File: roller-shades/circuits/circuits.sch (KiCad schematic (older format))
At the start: 24 parts, among them U1 AMS1117-3.3, U3 ESP-12F

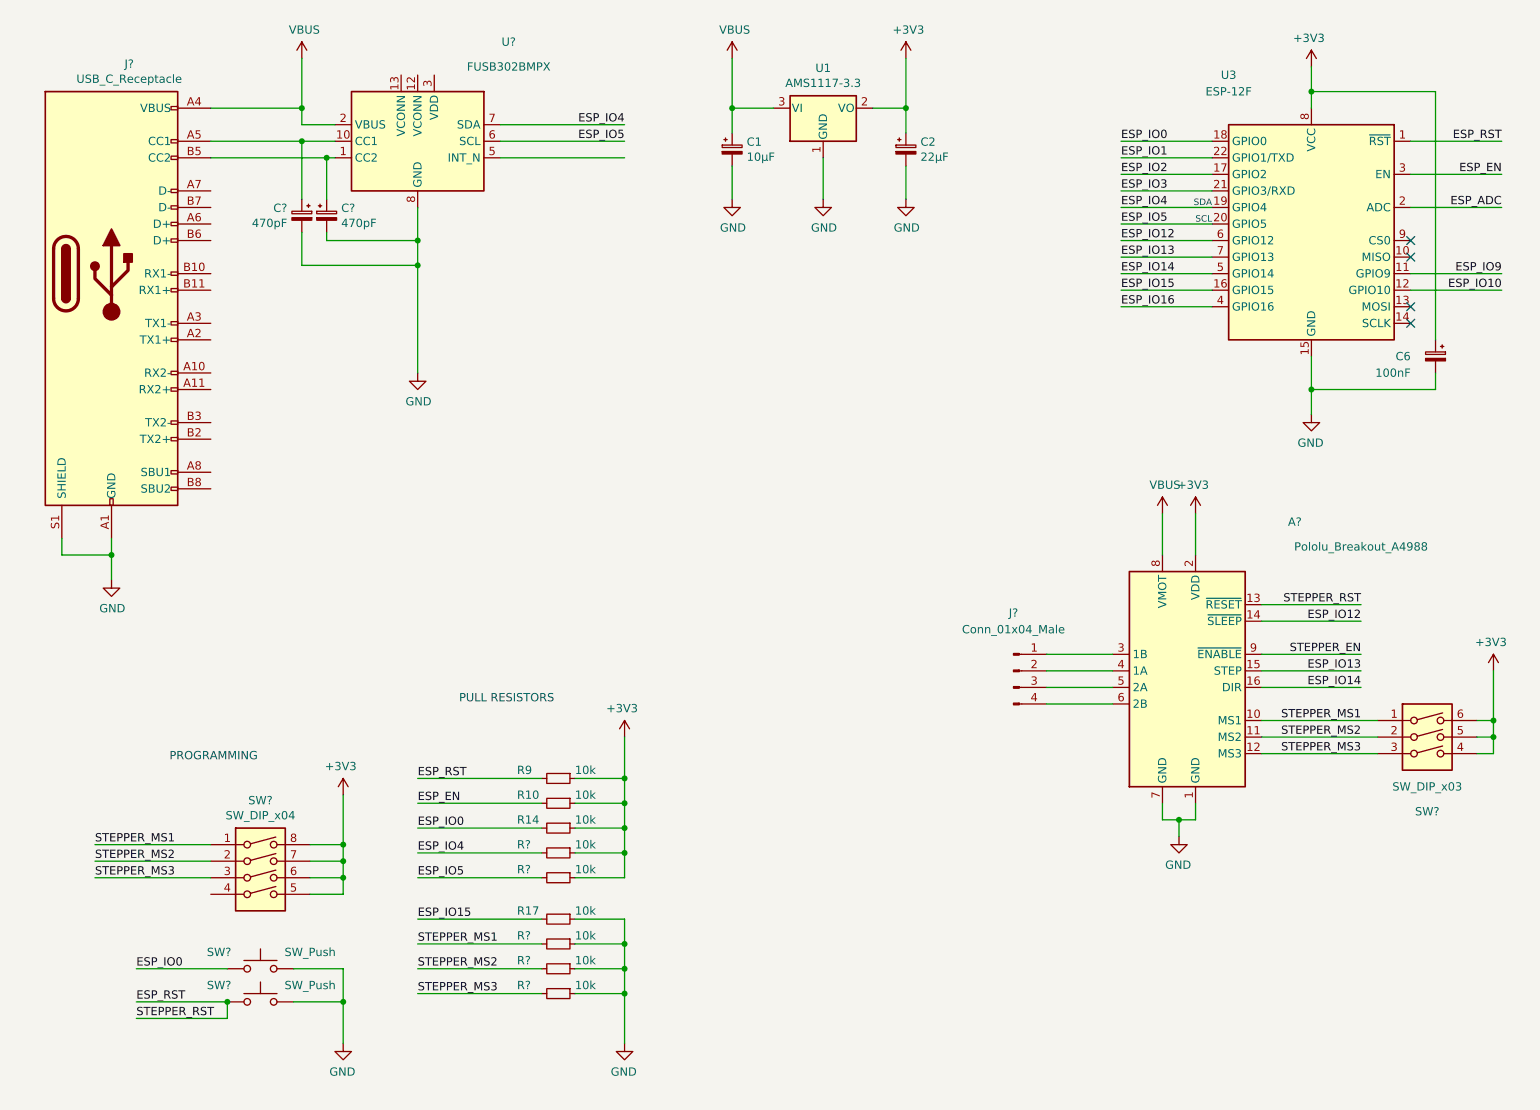
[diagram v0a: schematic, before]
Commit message: Refractored KiCAD repo libraries and added AS5601-ASOM
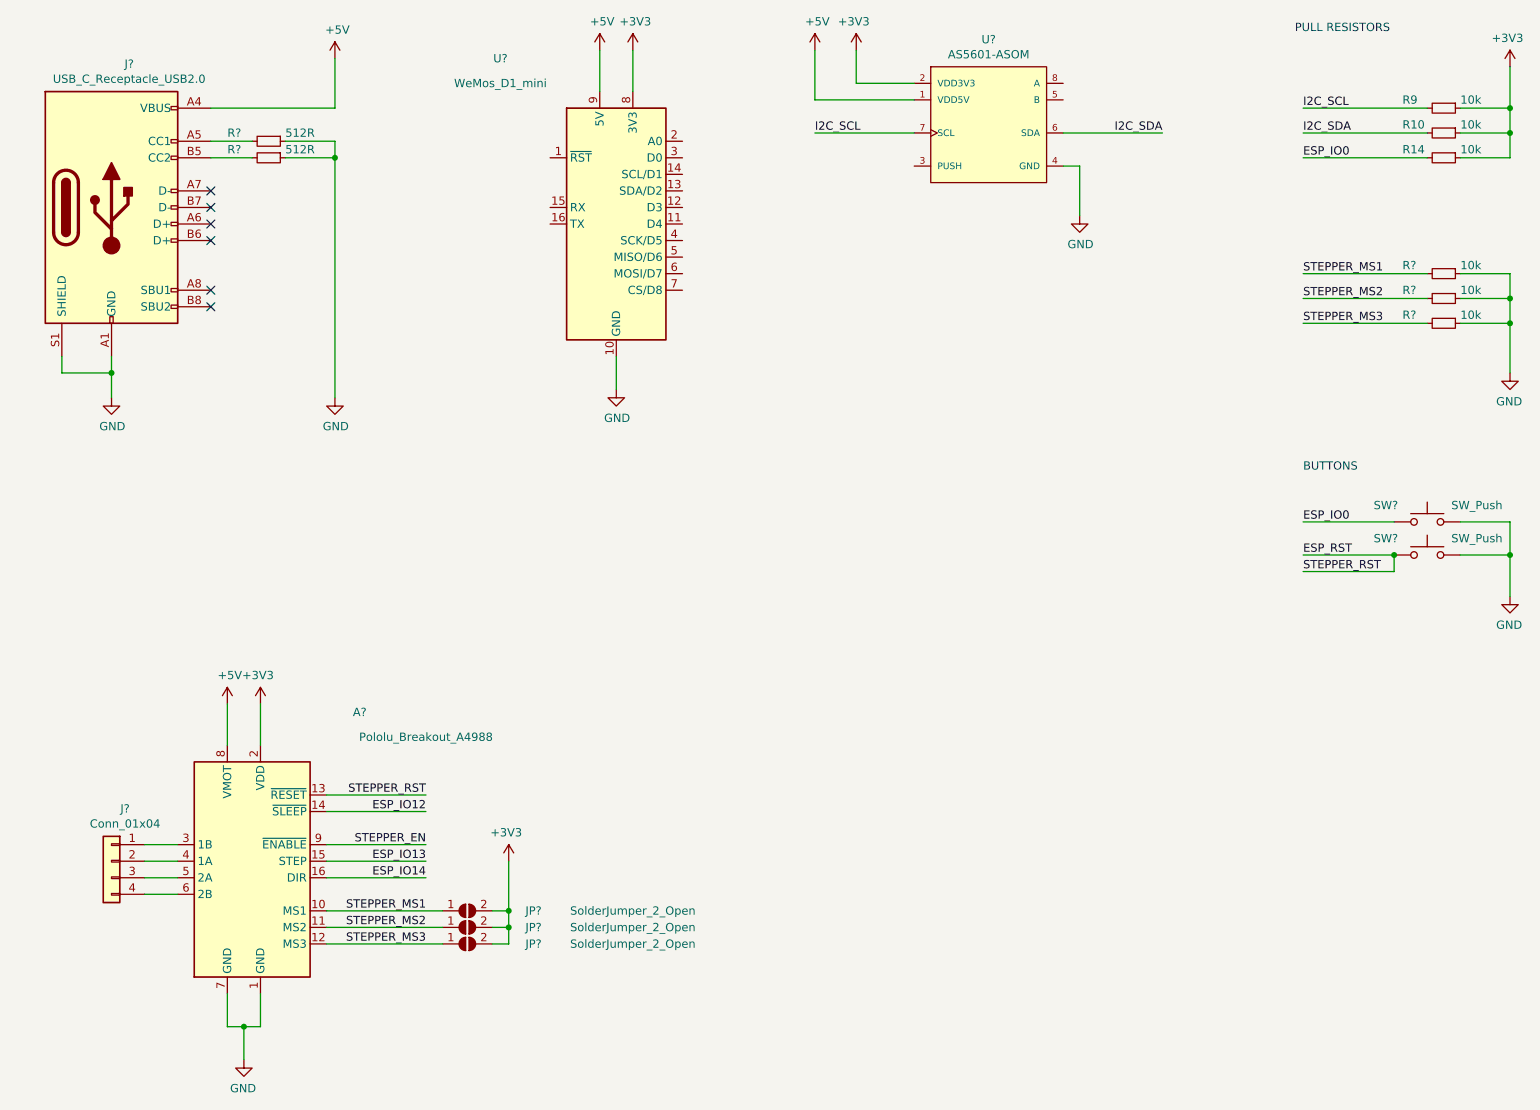
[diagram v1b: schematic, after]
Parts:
- removed C1: 10µF, Capacitor_SMD:C_1206_3216Metric, symbol Device:CP_Small
- removed C2: 22µF, Capacitor_SMD:C_1206_3216Metric, symbol Device:CP_Small
- removed C6: 100nF, Capacitor_SMD:C_1206_3216Metric, symbol Device:CP_Small
- removed C? (x2): 470pF, Capacitor_SMD:C_1206_3216Metric, symbol Device:CP_Small
- removed J?: Conn_01x04_Male, symbol Connector:Conn_01x04_Male
- removed J?: USB_C_Receptacle, symbol Connector:USB_C_Receptacle
- removed R17, R? (x2): 10k, Capacitor_SMD:C_1206_3216Metric, symbol Device:R_Small
- removed SW?: SW_DIP_x04, symbol Switch:SW_DIP_x04
- removed SW?: SW_DIP_x03, symbol Switch:SW_DIP_x03
- removed U1: AMS1117-3.3, Package_TO_SOT_SMD:SOT-223-3_TabPin2, symbol Regulator_Linear:AMS1117-3.3
- removed U3: ESP-12F, RF_Module:ESP-12E, symbol RF_Module:ESP-12F
- removed U?: FUSB302BMPX, Package_DFN_QFN:WQFN-14-1EP_2.5x2.5mm_P0.5mm_EP1.45x1.45mm, symbol Interface_USB:FUSB302BMPX
- added J?: USB_C_Receptacle_USB2.0, symbol Connector:USB_C_Receptacle_USB2.0
- added J?: Conn_01x04, symbol Connector_Generic:Conn_01x04
- added JP? (x3): SolderJumper_2_Open, symbol Jumper:SolderJumper_2_Open
- added R? (x2): 512R, Capacitor_SMD:C_1206_3216Metric, symbol Device:R_Small
- added U?: WeMos_D1_mini, Module:WEMOS_D1_mini_light, symbol MCU_Module:WeMos_D1_mini
- added U?: AS5601-ASOM, Taos-AS5601-ASOM-0-0-*, symbol AS5601:AS5601-ASOM
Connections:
- net +3V3: now also JP?.2 (B), JP?.2 (B), JP?.2 (B), U?.2 (VDD3V3), U?.8 (3V3)
- net ESP_RST: no longer R9.2
- net GND: now also J?.A1 (GND), J?.A12 (GND), J?.B1 (GND), J?.B12 (GND), J?.S1 (SHIELD), R?.1, R?.1, U?.10 (GND), U?.4 (GND)
- net STEPPER_MS1: now also JP?.1 (A)
- net STEPPER_MS2: now also JP?.1 (A)
- net STEPPER_MS3: now also JP?.1 (A)
- net at A?.3 (1B): now also J?.1 (Pin_1)
- net at A?.4 (1A): now also J?.2 (Pin_2)
- net at A?.5 (2A): now also J?.3 (Pin_3)
- net at A?.6 (2B): now also J?.4 (Pin_4)
- net ESP_EN renamed I2C_SDA
- net I2C_SDA: now also U?.6 (SDA)
- net VBUS renamed +5V
- net +5V: now also J?.A4 (VBUS), J?.A9 (VBUS), J?.B4 (VBUS), J?.B9 (VBUS), U?.1 (VDD5V), U?.9 (5V)
- new net: J?.A5 (CC1), R?.2
- new net: J?.B5 (CC2), R?.2
- new net I2C_SCL: R9.2, U?.7 (SCL)
- no-connect marks 4 -> 6
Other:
- note added: "BUTTONS"
- note removed: "PROGRAMMING"
- note removed: "SCL"
- note removed: "SDA"
- moved on the sheet: A?, R10, R14, R9, R?, SW?

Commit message: work on roller shade schmatics
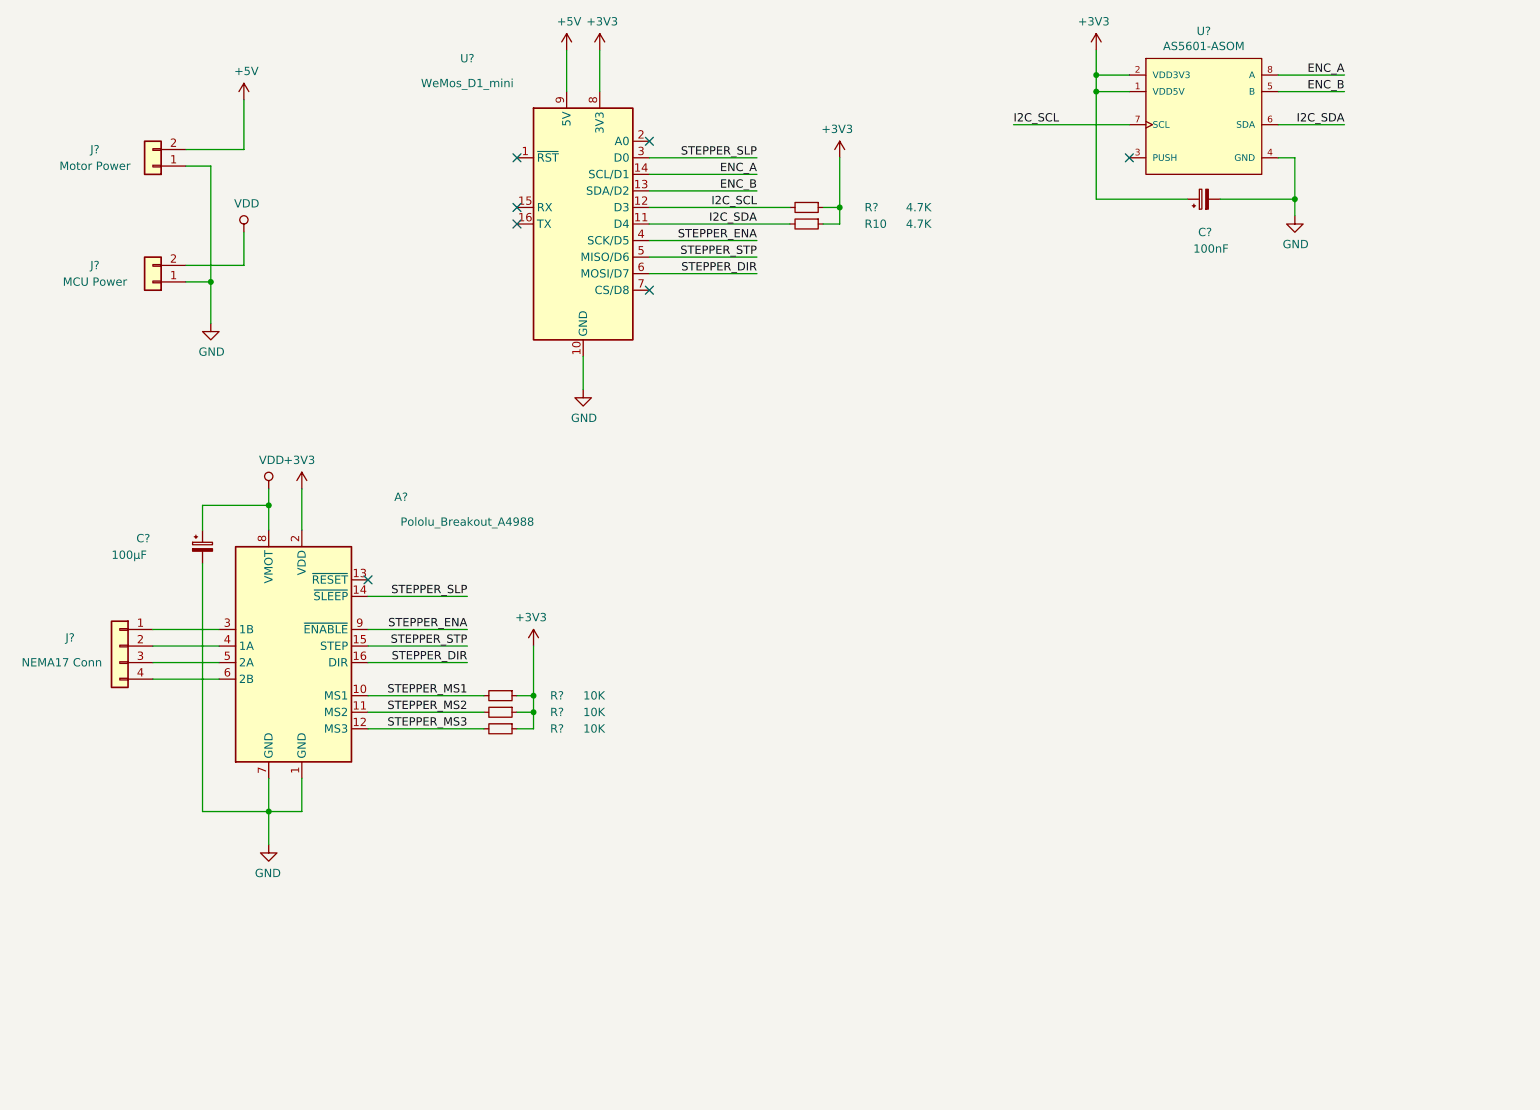
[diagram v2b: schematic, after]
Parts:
- removed J?: USB_C_Receptacle_USB2.0, symbol Connector:USB_C_Receptacle_USB2.0
- removed JP? (x3): SolderJumper_2_Open, symbol Jumper:SolderJumper_2_Open
- removed R14, R9, R? (x3): 10k, Capacitor_SMD:C_1206_3216Metric, symbol Device:R_Small
- removed R? (x2): 512R, Capacitor_SMD:C_1206_3216Metric, symbol Device:R_Small
- removed SW? (x2): SW_Push, symbol Switch:SW_Push
- added C?: 100µF, symbol Device:CP_Small
- added C?: 100nF, symbol Device:CP_Small
- added J?: Motor Power, symbol Connector_Generic:Conn_01x02
- added J?: MCU Power, symbol Connector_Generic:Conn_01x02
- added R?: 4.7K, Capacitor_SMD:C_1206_3216Metric, symbol Device:R_Small
- added R? (x3): 10K, Capacitor_SMD:C_1206_3216Metric, symbol Device:R_Small
- J?: value Conn_01x04 -> NEMA17 Conn
- R10: value 10k -> 4.7K
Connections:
- net ESP_IO12 is gone; now on net STEPPER_SLP: A?.14 (~SLEEP)
- net ESP_IO13 is gone; now on net STEPPER_STP: A?.15 (STEP)
- net ESP_IO14 is gone; now on net STEPPER_DIR: A?.16 (DIR)
- net STEPPER_EN is gone; now on net STEPPER_ENA: A?.9 (~ENABLE)
- net +3V3: now also U?.1 (VDD5V), C?.1, R?.1, R?.1, R?.1, R?.1
- net +5V: now also J?.2 (Pin_2); no longer A?.8 (VMOT), U?.1 (VDD5V)
- net GND: now also C?.2, C?.2, J?.1 (Pin_1), J?.1 (Pin_1)
- net I2C_SCL: now also U?.12 (D3), R?.2
- net I2C_SDA: now also U?.11 (D4)
- net STEPPER_MS1: now also R?.2
- net STEPPER_MS2: now also R?.2
- net STEPPER_MS3: now also R?.2
- net ENC_B: now reaches U?.13 (SDA/D2)
- net ENC_B: now also U?.5 (B)
- net ENC_A: now reaches U?.14 (SCL/D1)
- net ENC_A: now also U?.8 (A)
- net STEPPER_SLP: now reaches U?.3 (D0)
- net STEPPER_ENA: now reaches U?.4 (SCK/D5)
- net STEPPER_STP: now reaches U?.5 (MISO/D6)
- net STEPPER_DIR: now reaches U?.6 (MOSI/D7)
- net ESP_RST: no longer names the net of A?.13 (~RESET)
- new net VDD: A?.8 (VMOT), C?.1, J?.2 (Pin_2)
- no-connect marks 6 -> 7
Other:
- note removed: "BUTTONS"
- note removed: "PULL RESISTORS"
- moved on the sheet: A?, J?, R10, U?

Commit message: working on driver board using kicad stepup for freecad
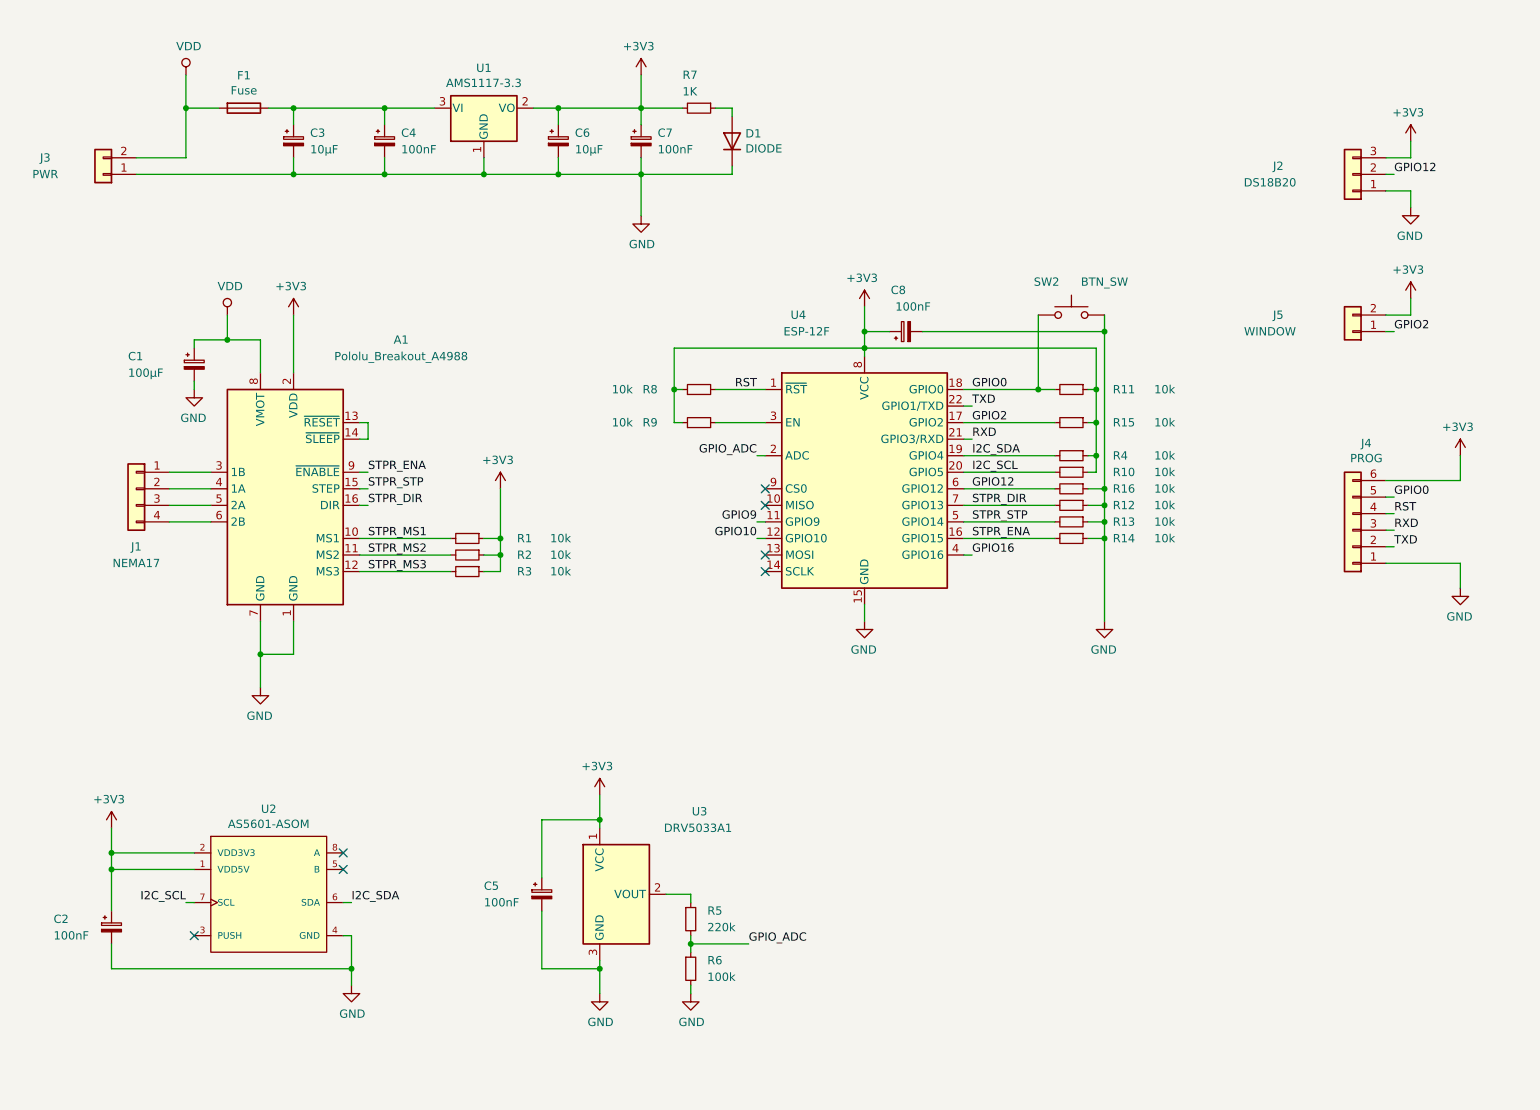
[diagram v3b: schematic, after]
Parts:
- removed J?: Motor Power, symbol Connector_Generic:Conn_01x02
- removed U?: WeMos_D1_mini, Module:WEMOS_D1_mini_light, symbol MCU_Module:WeMos_D1_mini
- added C3, C6: 10µF, Capacitor_SMD:C_0603_1608Metric, symbol Device:CP_Small
- added C4, C5, C7: 100nF, Capacitor_SMD:C_0603_1608Metric, symbol Device:CP_Small
- added C8: 100nF, Fuse:Fuse_0805_2012Metric, symbol Device:CP_Small
- added D1: DIODE, Diode_SMD:D_0805_2012Metric, symbol Simulation_SPICE:DIODE
- added F1: Fuse, Fuse:Fuse_0603_1608Metric, symbol Device:Fuse
- added J2: DS18B20, Connector_PinSocket_2.00mm:PinSocket_1x03_P2.00mm_Vertical, symbol Connector_Generic:Conn_01x03
- added J4: PROG, Connector_PinHeader_2.00mm:PinHeader_1x06_P2.00mm_Vertical, symbol Connector_Generic:Conn_01x06
- added J5: WINDOW, Connector_PinHeader_2.54mm:PinHeader_1x02_P2.54mm_Vertical, symbol Connector_Generic:Conn_01x02
- added R11, R12, R13, R14, R15, R16, R8, R9: 10k, Resistor_SMD:R_0603_1608Metric, symbol Device:R_Small
- added R5: 220k, Resistor_SMD:R_0603_1608Metric, symbol Device:R_Small
- added R6: 100k, Resistor_SMD:R_0603_1608Metric, symbol Device:R_Small
- added R7: 1K, Resistor_SMD:R_0603_1608Metric, symbol Device:R_Small
- added SW2: BTN_SW, Button_Switch_SMD:SW_DIP_SPSTx01_Slide_Copal_CHS-01A_W5.08mm_P1.27mm_JPin, symbol Switch:SW_Push
- added U1: AMS1117-3.3, Package_TO_SOT_SMD:SOT-223-3_TabPin2, symbol Regulator_Linear:AMS1117-3.3
- added U3: DRV5033A1, Package_TO_SOT_THT:TO-92Flat, symbol Sensor_Magnetic:DRV5033AJQDBZ
- added U4: ESP-12F, RF_Module:ESP-12E, symbol RF_Module:ESP-12F
- C1: renamed from C?; footprint (none) -> Capacitor_SMD:CP_Elec_6.3x7.7
- C2: renamed from C?; footprint (none) -> Capacitor_SMD:C_0603_1608Metric
- J1: renamed from J?; value NEMA17 Conn -> NEMA17; footprint (none) -> Connector_PinHeader_2.54mm:PinHeader_1x04_P2.54mm_Vertical
- J3: renamed from J?; value MCU Power -> PWR; footprint (none) -> Connector_PinHeader_2.54mm:PinHeader_1x02_P2.54mm_Vertical
- R1, R2, R3: renamed from R?; value 10K -> 10k; footprint Capacitor_SMD:C_1206_3216Metric -> Resistor_SMD:R_0603_1608Metric
- R10: value 4.7K -> 10k; footprint Capacitor_SMD:C_1206_3216Metric -> Resistor_SMD:R_0603_1608Metric
- R4: renamed from R?; value 4.7K -> 10k; footprint Capacitor_SMD:C_1206_3216Metric -> Resistor_SMD:R_0603_1608Metric
- U2: renamed from U?; footprint Taos-AS5601-ASOM-0-0-* -> AS5601:Taos-AS5601-ASOM-0-0-0
- gave numbers to parts that had none: 1
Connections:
- net STEPPER_SLP is gone; now on an unnamed net: A1.14 (~SLEEP)
- net +3V3: now also C5.1, C6.1, C7.1, C8.1, J2.3 (Pin_3), J4.6 (Pin_6), J5.2 (Pin_2), R11.1, R15.1, R7.2, R8.1, R9.1, U1.2 (VO), U3.1 (VCC), U4.8 (VCC)
- net GND: now also C3.2, C4.2, C5.2, C6.2, C7.2, C8.2, D1.2 (K), J2.1 (Pin_1), J4.1 (Pin_1), R12.1, R13.1, R14.1, R16.1, R6.2, SW2.2, U1.1 (GND), U3.3 (GND), U4.15 (GND)
- net I2C_SCL: now also R10.2, U4.20 (GPIO5); no longer R4.2
- net I2C_SDA: now also R4.2, U4.19 (GPIO4); no longer R10.2
- net VDD: now also F1.2
- net ENC_A: no longer names the net of U2.8 (A)
- net ENC_B: no longer names the net of U2.5 (B)
- net STEPPER_DIR renamed STPR_DIR
- net STPR_DIR: now also R12.2, U4.7 (GPIO13)
- net STEPPER_ENA renamed STPR_ENA
- net STPR_ENA: now also R14.2, U4.16 (GPIO15)
- net STEPPER_MS1 renamed STPR_MS1
- net STEPPER_MS2 renamed STPR_MS2
- net STEPPER_MS3 renamed STPR_MS3
- net STEPPER_STP renamed STPR_STP
- net STPR_STP: now also R13.2, U4.5 (GPIO14)
- new net: R9.2, U4.3 (EN)
- new net: C3.1, C4.1, F1.1, U1.3 (VI)
- new net: D1.1 (A), R7.1
- new net: R5.1, U3.2 (VOUT)
- new net GPIO0: J4.5 (Pin_5), R11.2, SW2.1, U4.18 (GPIO0)
- new net GPIO10: U4.12 (GPIO10)
- new net GPIO12: J2.2 (Pin_2), R16.2, U4.6 (GPIO12)
- new net GPIO16: U4.4 (GPIO16)
- new net GPIO2: J5.1 (Pin_1), R15.2, U4.17 (GPIO2)
- new net GPIO9: U4.11 (GPIO9)
- new net GPIO_ADC: R5.2, R6.1, U4.2 (ADC)
- new net RST: J4.4 (Pin_4), R8.2, U4.1 (~RST)
- new net RXD: J4.3 (Pin_3), U4.21 (GPIO3/RXD)
- new net TXD: J4.2 (Pin_2), U4.22 (GPIO1/TXD)
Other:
- moved on the sheet: A1, C1, C2, J1, J3, R1, R10, R2, R3, R4, U2
